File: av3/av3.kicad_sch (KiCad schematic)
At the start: 0 parts

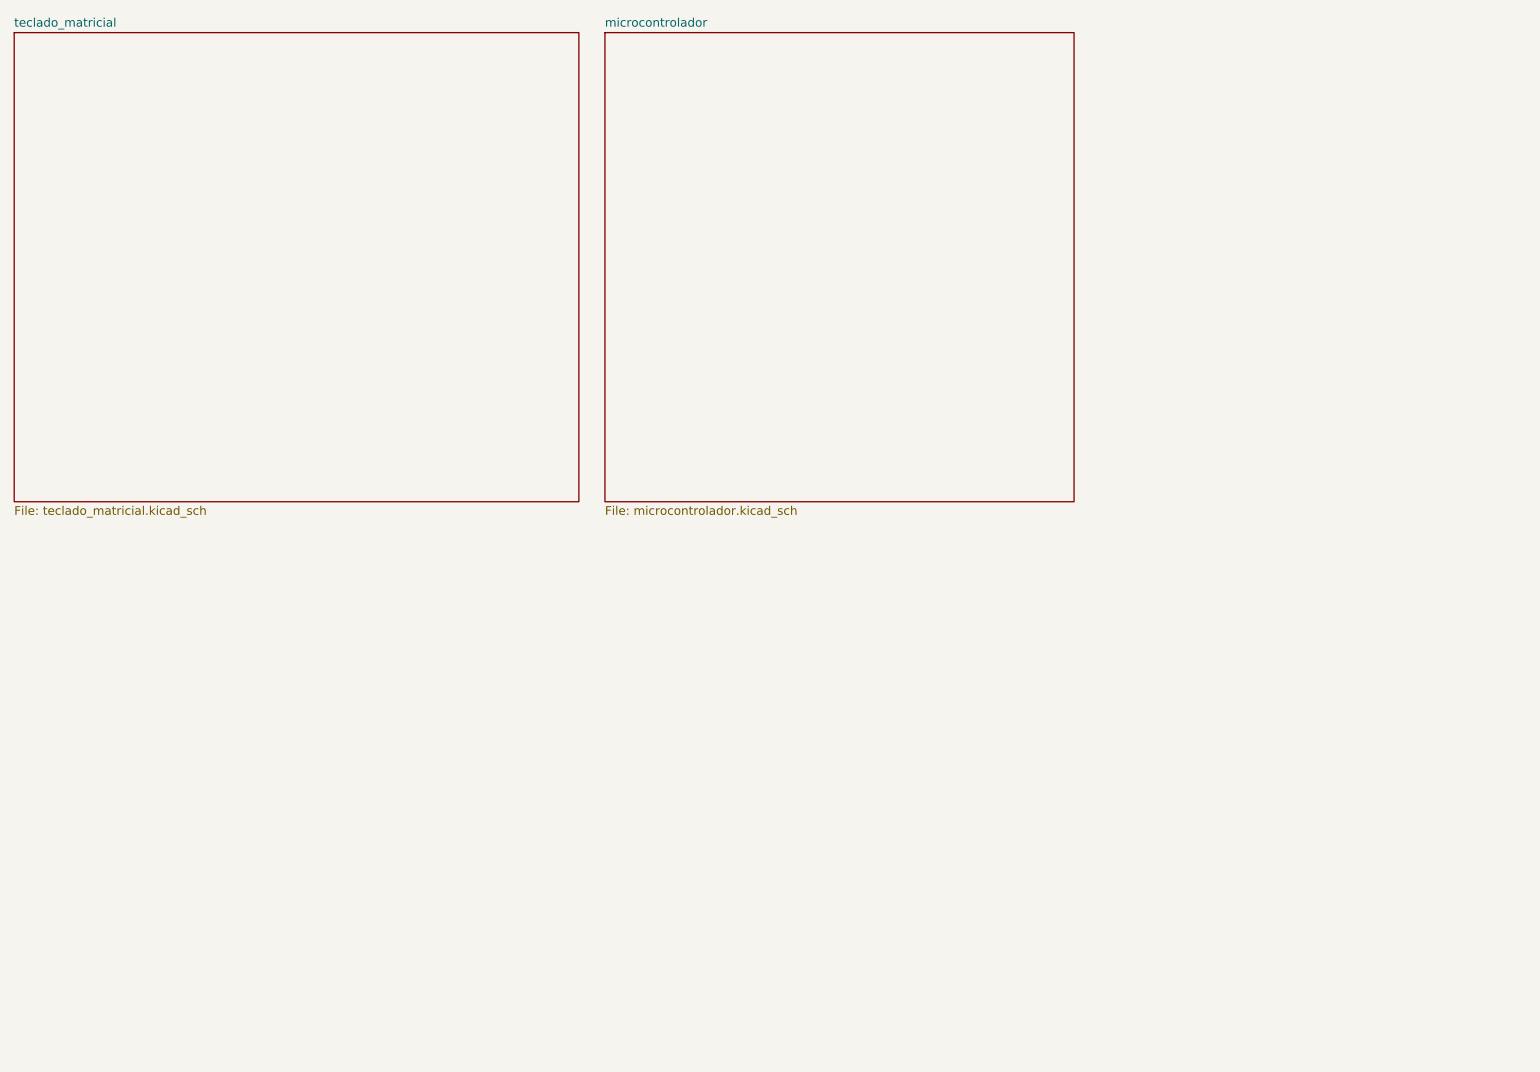
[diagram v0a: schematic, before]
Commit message: FEAT: Adiciona as folhas de projeto restantes (reles, modulo_entrada e condicionamento_sinal)
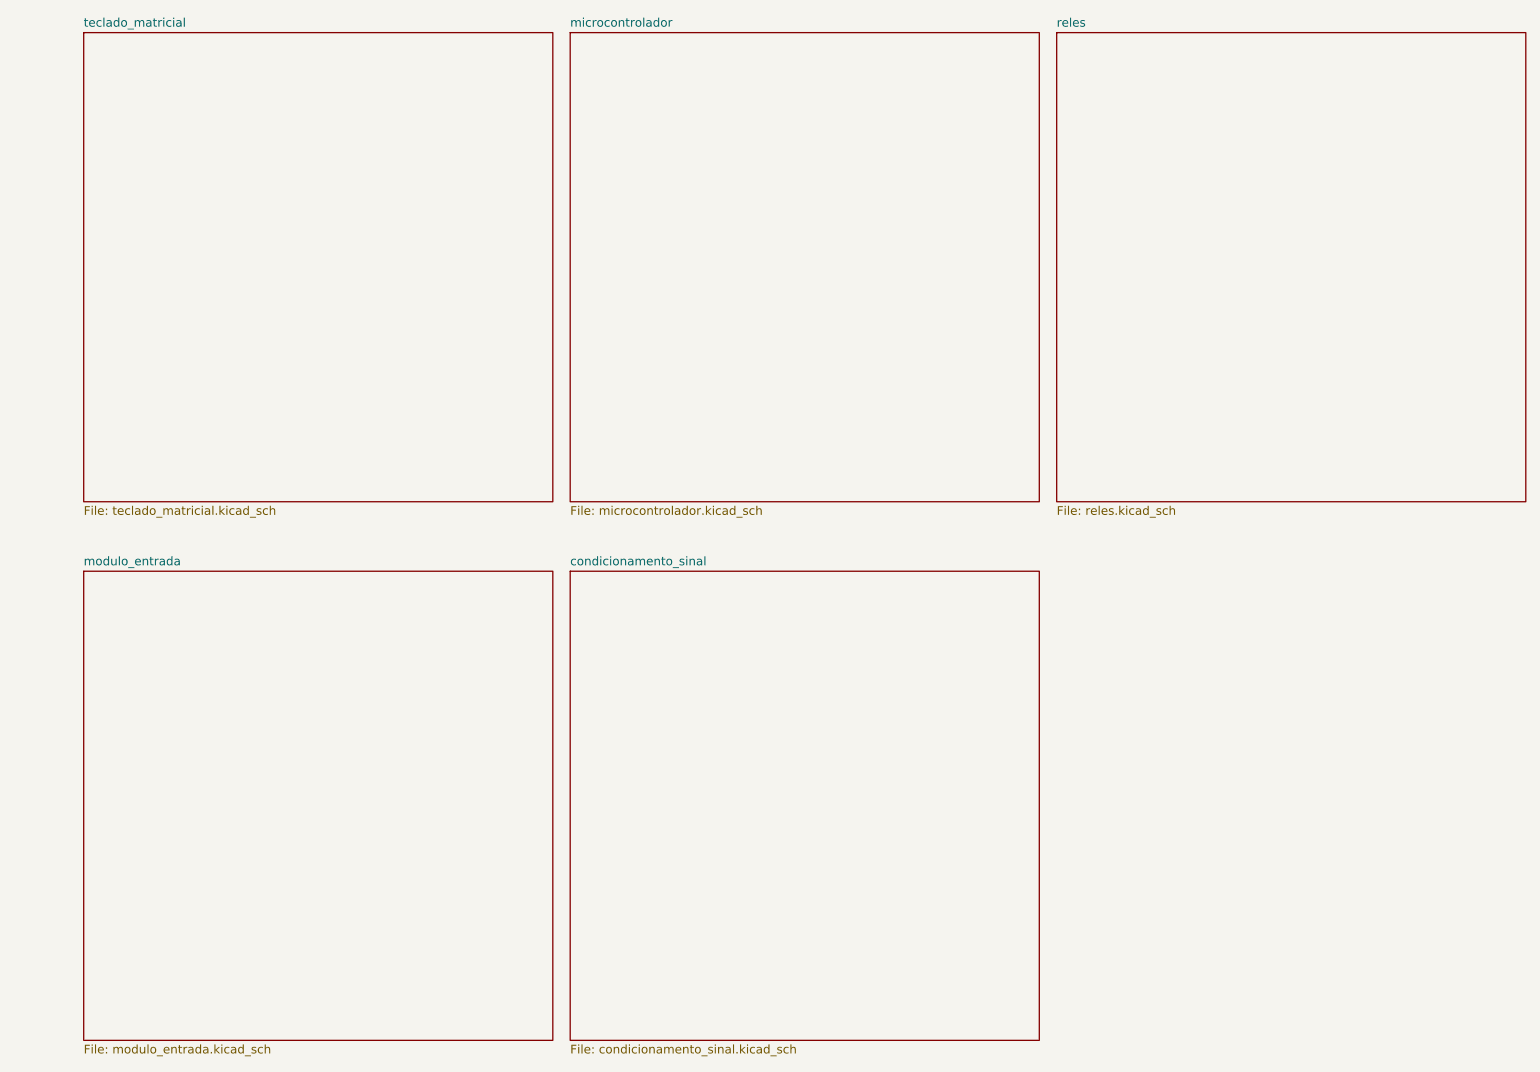
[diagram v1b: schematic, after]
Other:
- added sheet condicionamento_sinal (condicionamento_sinal.kicad_sch)
- added sheet modulo_entrada (modulo_entrada.kicad_sch)
- added sheet reles (reles.kicad_sch)
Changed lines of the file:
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@@
 	(paper "A4")
 	(sheet
-		(at 16.51 17.78)
-		(size 82.55 68.58)
+		(at 26.67 96.52)
+		(size 68.58 68.58)
+		(exclude_from_sim no)
+		(in_bom yes)
+		(on_board yes)
+		(dnp no)
+		(fields_autoplaced yes)
+		(stroke
+			(width 0.1524)
+			(type solid)
+		)
+		(fill
+			(color 0 0 0 0.0000)
+		)
+		(property "Sheetname" "modulo_entrada"
+			(at 26.67 95.8084 0)
+			(effects
+				(font
+					(size 1.27 1.27)
+				)
+				(justify left bottom)
+			)
+		)
+		(property "Sheetfile" "modulo_entrada.kicad_sch"
+			(at 26.67 165.6846 0)
+			(effects
+				(font
+					(size 1.27 1.27)
+				)
+				(justify left top)
+			)
+		)
+		(instances
+			(project "av3"
+				(path "/a93ad2d2-2340-43ed-bd19-332540d0678c"
+					(page "5")
+				)
+			)
+		)
+	)
+	(sheet
+		(at 97.79 96.52)
+		(size 68.58 68.58)
+		(exclude_from_sim no)
+		(in_bom yes)
+		(on_board yes)
+		(dnp no)
+		(fields_autoplaced yes)
+		(stroke
+			(width 0.1524)
+			(type solid)
+		)
+		(fill
+			(color 0 0 0 0.0000)
+		)
+		(property "Sheetname" "condicionamento_sinal"
+			(at 97.79 95.8084 0)
+			(effects
+				(font
+					(size 1.27 1.27)
+				)
+				(justify left bottom)
+			)
+		)
+		(property "Sheetfile" "condicionamento_sinal.kicad_sch"
+			(at 97.79 165.6846 0)
+			(effects
+				(font
+					(size 1.27 1.27)
+				)
+				(justify left top)
+			)
+		)
+		(instances
+			(project "av3"
+				(path "/a93ad2d2-2340-43ed-bd19-332540d0678c"
+					(page "6")
+				)
+			)
+		)
+	)
+	(sheet
+		(at 168.91 17.78)
+		(size 68.58 68.58)
+		(exclude_from_sim no)
+		(in_bom yes)
+		(on_board yes)
+		(dnp no)
+		(fields_autoplaced yes)
+		(stroke
+			(width 0.1524)
+			(type solid)
+		)
+		(fill
+			(color 0 0 0 0.0000)
+		)
+		(property "Sheetname" "reles"
+			(at 168.91 17.0684 0)
+			(effects
+				(font
+					(size 1.27 1.27)
+				)
+				(justify left bottom)
+			)
+		)
+		(property "Sheetfile" "reles.kicad_sch"
+			(at 168.91 86.9446 0)
+			(effects
+				(font
+					(size 1.27 1.27)
+				)
+				(justify left top)
+			)
+		)
+		(instances
+			(project "av3"
+				(path "/a93ad2d2-2340-43ed-bd19-332540d0678c"
+					(page "4")
+				)
+			)
+		)
+	)
+	(sheet
+		(at 26.67 17.78)
+		(size 68.58 68.58)
 		(exclude_from_sim no)
 		(in_bom yes)
@@
 		)
 		(property "Sheetname" "teclado_matricial"
-			(at 16.51 17.0684 0)
+			(at 26.67 17.0684 0)
 			(effects
 				(font
@@
 		)
 		(property "Sheetfile" "teclado_matricial.kicad_sch"
-			(at 16.51 86.9446 0)
+			(at 26.67 86.9446 0)
 			(effects
 				(font
@@
 	)
 	(sheet
-		(at 102.87 17.78)
+		(at 97.79 17.78)
 		(size 68.58 68.58)
 		(exclude_from_sim no)
@@
 		)
 		(property "Sheetname" "microcontrolador"
-			(at 102.87 17.0684 0)
+			(at 97.79 17.0684 0)
 			(effects
 				(font
@@
 		)
 		(property "Sheetfile" "microcontrolador.kicad_sch"
-			(at 102.87 86.9446 0)
+			(at 97.79 86.9446 0)
 			(effects
 				(font
